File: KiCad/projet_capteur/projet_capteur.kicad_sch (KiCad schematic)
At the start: 5 parts, among them J1 Power, J2 Digital/PWM, J3 Analog, J4 Digital/PWM

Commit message: Ajout FlexSensor
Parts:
- added U2: ~, Lib_empreint:Empreinte_FlexSensor, symbol Ma_lib_graphique:model_FlexSensor
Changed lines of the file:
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@@
+	)
+	(symbol
+		(lib_id "Ma_lib_graphique:model_FlexSensor")
+		(at 113.03 50.8 0)
+		(unit 1)
+		(exclude_from_sim no)
+		(in_bom yes)
+		(on_board yes)
+		(dnp no)
+		(fields_autoplaced yes)
+		(property "Reference" "U2"
+			(at 120.65 44.4499 0)
+			(effects
+				(font
+					(size 1.27 1.27)
+				)
+				(justify left)
+			)
+		)
+		(property "Value" "~"
+			(at 120.65 46.355 0)
+			(effects
+				(font
+					(size 1.27 1.27)
+				)
+				(justify left)
+			)
+		)
+		(property "Footprint" "Lib_empreint:Empreinte_FlexSensor"
+			(at 113.03 50.8 0)
+			(effects
+				(font
+					(size 1.27 1.27)
+				)
+				(hide yes)
+			)
+		)
+		(property "Datasheet" ""
+			(at 113.03 50.8 0)
+			(effects
+				(font
+					(size 1.27 1.27)
+				)
+				(hide yes)
+			)
+		)
+		(property "Description" ""
+			(at 113.03 50.8 0)
+			(effects
+				(font
+					(size 1.27 1.27)
+				)
+				(hide yes)
+			)
+		)
+		(pin "1"
+		)
+		(pin "2"
+		)
+		(instances
+			(project ""
+				(path "/e63e39d7-6ac0-4ffd-8aa3-1841a4541b55"
+					(reference "U2")
+					(unit 1)
+				)
+			)
+		)
 	)
 	(symbol

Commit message: Add bluetooth and encoder symbol into Schematic
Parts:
- removed U2: ~, Lib_empreint:Empreinte_FlexSensor, symbol Ma_lib_graphique:model_FlexSensor
- added U2: ~, symbol Ma_lib_graphique:model_Bluetooth
- added U3: ~, symbol Ma_lib_graphique:model_Rotary_Encoder
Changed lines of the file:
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@@
 	)
 	(symbol
-		(lib_id "Ma_lib_graphique:model_FlexSensor")
-		(at 113.03 50.8 0)
+		(lib_id "Ma_lib_graphique:model_Bluetooth")
+		(at 158.75 44.45 0)
 		(unit 1)
 		(exclude_from_sim no)
@@
 		(fields_autoplaced yes)
 		(property "Reference" "U2"
-			(at 120.65 44.4499 0)
+			(at 170.18 31.1149 0)
 			(effects
 				(font
@@
 		)
 		(property "Value" "~"
-			(at 120.65 46.355 0)
+			(at 170.18 33.02 0)
 			(effects
 				(font
@@
 			)
 		)
-		(property "Footprint" "Lib_empreint:Empreinte_FlexSensor"
-			(at 113.03 50.8 0)
+		(property "Footprint" ""
+			(at 158.75 44.45 0)
 			(effects
 				(font
@@
 		)
 		(property "Datasheet" ""
-			(at 113.03 50.8 0)
+			(at 158.75 44.45 0)
 			(effects
 				(font
@@
 		)
 		(property "Description" ""
-			(at 113.03 50.8 0)
+			(at 158.75 44.45 0)
 			(effects
 				(font
@@
 			)
 		)
+		(pin "5"
+		)
+		(pin "6"
+		)
+		(pin "3"
+		)
 		(pin "1"
 		)
 		(pin "2"
+		)
+		(pin "4"
 		)
 		(instances
@@
 					(unit 1)
 				)
+			)
+		)
+	)
+	(symbol
+		(lib_id "Ma_lib_graphique:model_Rotary_Encoder")
+		(at 189.23 36.83 0)
+		(unit 1)
+		(exclude_from_sim no)
+		(in_bom yes)
+		(on_board yes)
+		(dnp no)
+		(fields_autoplaced yes)
+		(property "Reference" "U3"
+			(at 198.12 27.9399 0)
+			(effects
+				(font
+					(size 1.27 1.27)
+				)
+				(justify left)
+			)
+		)
+		(property "Value" "~"
+			(at 198.12 29.845 0)
+			(effects
+				(font
+					(size 1.27 1.27)
+				)
+				(justify left)
+			)
+		)
+		(property "Footprint" ""
+			(at 189.23 36.83 0)
+			(effects
+				(font
+					(size 1.27 1.27)
+				)
+				(hide yes)
+			)
+		)
+		(property "Datasheet" ""
+			(at 189.23 36.83 0)
+			(effects
+				(font
+					(size 1.27 1.27)
+				)
+				(hide yes)
+			)
+		)
+		(property "Description" ""
+			(at 189.23 36.83 0)
+			(effects
+				(font
+					(size 1.27 1.27)
+				)
+				(hide yes)
+			)
+		)
+		(pin "5"
+		)
+		(pin "2"
+		)
+		(pin "3"
+		)
+		(pin "4"
+		)
+		(pin "1"
+		)
+		(instances
+			(project ""
+				(path "/e63e39d7-6ac0-4ffd-8aa3-1841a4541b55"
+					(reference "U3")
+					(unit 1)
+				)

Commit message: Ajout symbole FlexSensor
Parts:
- added U4: ~, Lib_empreint:Empreinte_FlexSensor, symbol Ma_lib_graphique:model_FlexSensor
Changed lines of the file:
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@@
+	)
+	(symbol
+		(lib_id "Ma_lib_graphique:model_FlexSensor")
+		(at 114.3 60.96 0)
+		(unit 1)
+		(exclude_from_sim no)
+		(in_bom yes)
+		(on_board yes)
+		(dnp no)
+		(fields_autoplaced yes)
+		(property "Reference" "U4"
+			(at 121.92 54.6099 0)
+			(effects
+				(font
+					(size 1.27 1.27)
+				)
+				(justify left)
+			)
+		)
+		(property "Value" "~"
+			(at 121.92 56.515 0)
+			(effects
+				(font
+					(size 1.27 1.27)
+				)
+				(justify left)
+			)
+		)
+		(property "Footprint" "Lib_empreint:Empreinte_FlexSensor"
+			(at 114.3 60.96 0)
+			(effects
+				(font
+					(size 1.27 1.27)
+				)
+				(hide yes)
+			)
+		)
+		(property "Datasheet" ""
+			(at 114.3 60.96 0)
+			(effects
+				(font
+					(size 1.27 1.27)
+				)
+				(hide yes)
+			)
+		)
+		(property "Description" ""
+			(at 114.3 60.96 0)
+			(effects
+				(font
+					(size 1.27 1.27)
+				)
+				(hide yes)
+			)
+		)
+		(pin "1"
+		)
+		(pin "2"
+		)
+		(instances
+			(project ""
+				(path "/e63e39d7-6ac0-4ffd-8aa3-1841a4541b55"
+					(reference "U4")
+					(unit 1)
+				)
+			)
+		)
 	)
 	(symbol

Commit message: Modification OLED
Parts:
- U1: footprint Lib_empreint:SIP-4 -> Lib_empreint:Empreinte_OLED
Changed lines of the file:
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@@
 			)
 		)
-		(property "Footprint" "Lib_empreint:SIP-4"
+		(property "Footprint" "Lib_empreint:Empreinte_OLED"
 			(at 113.03 31.75 0)
 			(effects

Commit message: add symbol graphite sensor
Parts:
- added U5: ~, symbol Ma_lib_graphique:model_Graphite_Sensor
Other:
- moved on the sheet: U2, U3, U4
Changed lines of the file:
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@@
 	(symbol
 		(lib_id "Ma_lib_graphique:model_Bluetooth")
-		(at 158.75 44.45 0)
+		(at 142.24 44.45 0)
 		(unit 1)
 		(exclude_from_sim no)
@@
 		(fields_autoplaced yes)
 		(property "Reference" "U2"
-			(at 170.18 31.1149 0)
-			(effects
-				(font
-					(size 1.27 1.27)
-				)
-				(justify left)
-			)
-		)
-		(property "Value" "~"
-			(at 170.18 33.02 0)
+			(at 153.67 31.1149 0)
+			(effects
+				(font
+					(size 1.27 1.27)
+				)
+				(justify left)
+			)
+		)
+		(property "Value" "~"
+			(at 153.67 33.02 0)
 			(effects
 				(font
@@
 		)
 		(property "Footprint" ""
-			(at 158.75 44.45 0)
-			(effects
-				(font
-					(size 1.27 1.27)
-				)
-				(hide yes)
-			)
-		)
-		(property "Datasheet" ""
-			(at 158.75 44.45 0)
-			(effects
-				(font
-					(size 1.27 1.27)
-				)
-				(hide yes)
-			)
-		)
-		(property "Description" ""
-			(at 158.75 44.45 0)
+			(at 142.24 44.45 0)
+			(effects
+				(font
+					(size 1.27 1.27)
+				)
+				(hide yes)
+			)
+		)
+		(property "Datasheet" ""
+			(at 142.24 44.45 0)
+			(effects
+				(font
+					(size 1.27 1.27)
+				)
+				(hide yes)
+			)
+		)
+		(property "Description" ""
+			(at 142.24 44.45 0)
 			(effects
 				(font
@@
 	(symbol
 		(lib_id "Ma_lib_graphique:model_Rotary_Encoder")
-		(at 189.23 36.83 0)
+		(at 165.1 35.56 0)
 		(unit 1)
 		(exclude_from_sim no)
@@
 		(fields_autoplaced yes)
 		(property "Reference" "U3"
-			(at 198.12 27.9399 0)
-			(effects
-				(font
-					(size 1.27 1.27)
-				)
-				(justify left)
-			)
-		)
-		(property "Value" "~"
-			(at 198.12 29.845 0)
+			(at 173.99 26.6699 0)
+			(effects
+				(font
+					(size 1.27 1.27)
+				)
+				(justify left)
+			)
+		)
+		(property "Value" "~"
+			(at 173.99 28.575 0)
 			(effects
 				(font
@@
 		)
 		(property "Footprint" ""
-			(at 189.23 36.83 0)
-			(effects
-				(font
-					(size 1.27 1.27)
-				)
-				(hide yes)
-			)
-		)
-		(property "Datasheet" ""
-			(at 189.23 36.83 0)
-			(effects
-				(font
-					(size 1.27 1.27)
-				)
-				(hide yes)
-			)
-		)
-		(property "Description" ""
-			(at 189.23 36.83 0)
+			(at 165.1 35.56 0)
+			(effects
+				(font
+					(size 1.27 1.27)
+				)
+				(hide yes)
+			)
+		)
+		(property "Datasheet" ""
+			(at 165.1 35.56 0)
+			(effects
+				(font
+					(size 1.27 1.27)
+				)
+				(hide yes)
+			)
+		)
+		(property "Description" ""
+			(at 165.1 35.56 0)
 			(effects
 				(font
@@
 	)
 	(symbol
+		(lib_id "Ma_lib_graphique:model_Graphite_Sensor")
+		(at 205.74 31.75 0)
+		(unit 1)
+		(exclude_from_sim no)
+		(in_bom yes)
+		(on_board yes)
+		(dnp no)
+		(fields_autoplaced yes)
+		(property "Reference" "U5"
+			(at 209.55 24.7649 0)
+			(effects
+				(font
+					(size 1.27 1.27)
+				)
+				(justify left)
+			)
+		)
+		(property "Value" "~"
+			(at 209.55 26.67 0)
+			(effects
+				(font
+					(size 1.27 1.27)
+				)
+				(justify left)
+			)
+		)
+		(property "Footprint" ""
+			(at 205.74 31.75 0)
+			(effects
+				(font
+					(size 1.27 1.27)
+				)
+				(hide yes)
+			)
+		)
+		(property "Datasheet" ""
+			(at 205.74 31.75 0)
+			(effects
+				(font
+					(size 1.27 1.27)
+				)
+				(hide yes)
+			)
+		)
+		(property "Description" ""
+			(at 205.74 31.75 0)
+			(effects
+				(font
+					(size 1.27 1.27)
+				)
+				(hide yes)
+			)
+		)
+		(pin "1"
+		)
+		(pin "2"
+		)
+		(instances
+			(project ""
+				(path "/e63e39d7-6ac0-4ffd-8aa3-1841a4541b55"
+					(reference "U5")
+					(unit 1)
+				)
+			)
+		)
+	)
+	(symbol
 		(lib_id "Ma_lib_graphique:model_FlexSensor")
-		(at 114.3 60.96 0)
+		(at 186.69 27.94 0)
 		(unit 1)
 		(exclude_from_sim no)
@@
 		(fields_autoplaced yes)
 		(property "Reference" "U4"
-			(at 121.92 54.6099 0)
-			(effects
-				(font
-					(size 1.27 1.27)
-				)
-				(justify left)
-			)
-		)
-		(property "Value" "~"
-			(at 121.92 56.515 0)
+			(at 194.31 21.5899 0)
+			(effects
+				(font
+					(size 1.27 1.27)
+				)
+				(justify left)
+			)
+		)
+		(property "Value" "~"
+			(at 194.31 23.495 0)
 			(effects
 				(font
@@
 		)
 		(property "Footprint" "Lib_empreint:Empreinte_FlexSensor"
-			(at 114.3 60.96 0)
-			(effects
-				(font
-					(size 1.27 1.27)
-				)
-				(hide yes)
-			)
-		)
-		(property "Datasheet" ""
-			(at 114.3 60.96 0)
-			(effects
-				(font
-					(size 1.27 1.27)
-				)
-				(hide yes)
-			)
-		)
-		(property "Description" ""
-			(at 114.3 60.96 0)
-			(effects
-				(font
+			(at 186.69 27.94 0)
+			(effects
+				(font
+					(size 1.27 1.27)
+				)
+				(hide yes)
+			)
+		)
+		(property "Datasheet" ""
+			(at 186.69 27.94 0)
+			(effects
+				(font
+					(size 1.27 1.27)
+				)
+				(hide yes)
+			)
+		)
+		(property "Description" ""
+			(at 186.69 27.94 0)
+			(effects
+				(font

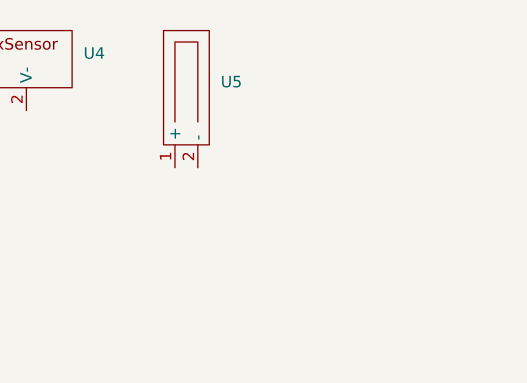
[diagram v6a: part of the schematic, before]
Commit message: add symbol LTC1050
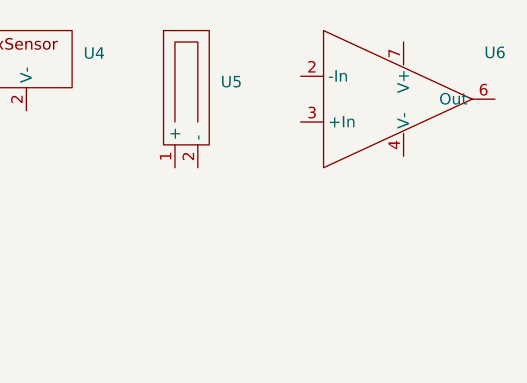
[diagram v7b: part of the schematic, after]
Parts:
- added U6: ~, symbol Ma_lib_graphique:model_LTC1050
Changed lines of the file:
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@@
+	)
+	(symbol
+		(lib_id "Ma_lib_graphique:model_LTC1050")
+		(at 228.6 26.67 0)
+		(unit 1)
+		(exclude_from_sim no)
+		(in_bom yes)
+		(on_board yes)
+		(dnp no)
+		(fields_autoplaced yes)
+		(property "Reference" "U6"
+			(at 240.03 21.5198 0)
+			(effects
+				(font
+					(size 1.27 1.27)
+				)
+			)
+		)
+		(property "Value" "~"
+			(at 240.03 23.4249 0)
+			(effects
+				(font
+					(size 1.27 1.27)
+				)
+			)
+		)
+		(property "Footprint" ""
+			(at 228.6 26.67 0)
+			(effects
+				(font
+					(size 1.27 1.27)
+				)
+				(hide yes)
+			)
+		)
+		(property "Datasheet" ""
+			(at 228.6 26.67 0)
+			(effects
+				(font
+					(size 1.27 1.27)
+				)
+				(hide yes)
+			)
+		)
+		(property "Description" ""
+			(at 228.6 26.67 0)
+			(effects
+				(font
+					(size 1.27 1.27)
+				)
+				(hide yes)
+			)
+		)
+		(pin "7"
+		)
+		(pin "3"
+		)
+		(pin "6"
+		)
+		(pin "4"
+		)
+		(pin "2"
+		)
+		(instances
+			(project ""
+				(path "/e63e39d7-6ac0-4ffd-8aa3-1841a4541b55"
+					(reference "U6")
+					(unit 1)
+				)
+			)
+		)
 	)
 	(symbol

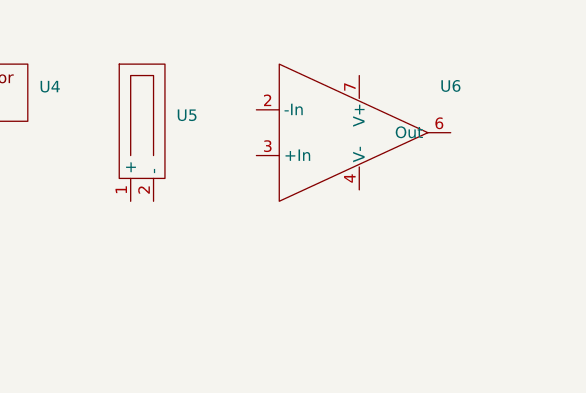
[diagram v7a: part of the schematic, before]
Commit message: add symbol LTC1050
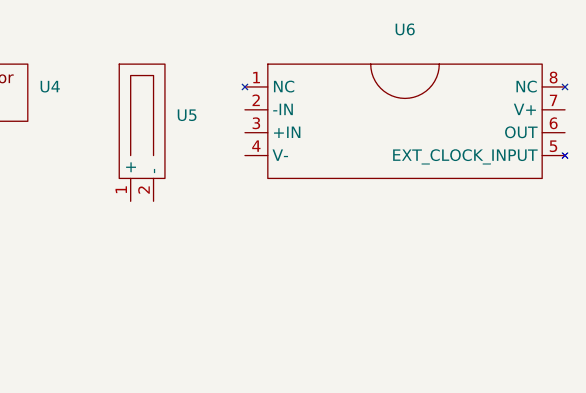
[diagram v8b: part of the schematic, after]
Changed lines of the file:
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@@
+	)
+	(symbol
+		(lib_id "Ma_lib_graphique:model_LTC1050")
+		(at 234.95 24.13 0)
+		(unit 1)
+		(exclude_from_sim no)
+		(in_bom yes)
+		(on_board yes)
+		(dnp no)
+		(fields_autoplaced yes)
+		(property "Reference" "U6"
+			(at 234.95 15.24 0)
+			(effects
+				(font
+					(size 1.27 1.27)
+				)
+			)
+		)
+		(property "Value" "~"
+			(at 234.95 17.78 0)
+			(effects
+				(font
+					(size 1.27 1.27)
+				)
+			)
+		)
+		(property "Footprint" ""
+			(at 234.95 24.13 0)
+			(effects
+				(font
+					(size 1.27 1.27)
+				)
+				(hide yes)
+			)
+		)
+		(property "Datasheet" ""
+			(at 234.95 24.13 0)
+			(effects
+				(font
+					(size 1.27 1.27)
+				)
+				(hide yes)
+			)
+		)
+		(property "Description" ""
+			(at 234.95 24.13 0)
+			(effects
+				(font
+					(size 1.27 1.27)
+				)
+				(hide yes)
+			)
+		)
+		(pin "6"
+		)
+		(pin "7"
+		)
+		(pin "8"
+		)
+		(pin "3"
+		)
+		(pin "1"
+		)
+		(pin "2"
+		)
+		(pin "4"
+		)
+		(pin "5"
+		)
+		(instances
+			(project ""
+				(path "/e63e39d7-6ac0-4ffd-8aa3-1841a4541b55"
+					(reference "U6")
+					(unit 1)
+				)
+			)
+		)
 	)
 	(symbol
@@
 					(unit 1)
 				)
-			)
-		)
-	)
-	(symbol
-		(lib_id "Ma_lib_graphique:model_LTC1050")
-		(at 228.6 26.67 0)
-		(unit 1)
-		(exclude_from_sim no)
-		(in_bom yes)
-		(on_board yes)
-		(dnp no)
-		(fields_autoplaced yes)
-		(property "Reference" "U6"
-			(at 240.03 21.5198 0)
-			(effects
-				(font
-					(size 1.27 1.27)
-				)
-			)
-		)
-		(property "Value" "~"
-			(at 240.03 23.4249 0)
-			(effects
-				(font
-					(size 1.27 1.27)
-				)
-			)
-		)
-		(property "Footprint" ""
-			(at 228.6 26.67 0)
-			(effects
-				(font
-					(size 1.27 1.27)
-				)
-				(hide yes)
-			)
-		)
-		(property "Datasheet" ""
-			(at 228.6 26.67 0)
-			(effects
-				(font
-					(size 1.27 1.27)
-				)
-				(hide yes)
-			)
-		)
-		(property "Description" ""
-			(at 228.6 26.67 0)
-			(effects
-				(font
-					(size 1.27 1.27)
-				)
-				(hide yes)
-			)
-		)
-		(pin "7"
-		)
-		(pin "3"
-		)
-		(pin "6"
-		)
-		(pin "4"
-		)
-		(pin "2"
-		)
-		(instances
-			(project ""
-				(path "/e63e39d7-6ac0-4ffd-8aa3-1841a4541b55"
-					(reference "U6")
-					(unit 1)
-				)
